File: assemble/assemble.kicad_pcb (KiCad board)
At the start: 2 copper layers, 94 parts, among them J1 Conn_01x04, SW1 SW_Push, SW10 SW_Push, SW11 SW_Push, SW12 SW_Push, SW13 SW_Push, SW14 SW_Push, SW15 SW_Push, SW16 SW_Push, SW17 SW_Push, SW18 SW_Push, SW19 SW_Push, SW2 SW_Push, SW20 SW_Push, SW21 SW_Push, SW22 SW_Push, SW23 SW_Push, SW24 SW_Push, SW25 SW_Push, SW26 SW_Push, SW27 SW_Push, SW28 SW_Push, SW29 SW_Push, SW3 SW_Push, SW30 SW_Push, SW31 SW_Push, SW32 SW_Push, SW33 SW_Push, SW34 SW_Push, SW35 SW_Push, SW36 SW_Push, SW37 SW_Push, SW38 SW_Push, SW39 SW_Push, SW4 SW_Push, SW40 SW_Push, SW41 SW_Push, SW42 SW_Push, SW44 SW_Push, SW45 RotaryEncoder_Switch, SW46 RotaryEncoder_Switch, SW47 SW_SPDT, SW5 SW_Push, SW6 SW_Push, SW7 SW_Push, SW8 SW_Push, SW9 SW_Push

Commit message: feat: re-annotation
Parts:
- moved D1 9.35 mm to (140.9, 58.8), turned to 165 degrees
- moved D5 8.33 mm to (124.9, 52.1), turned to 165 degrees
- moved SW1 8.27 mm to (139.6, 63.8), turned to 165 degrees
- moved SW5 6.84 mm to (123.6, 57.7), turned to 165 degrees
- moved D4 6.68 mm to (136.6, 108.9), turned to 175 degrees
- moved D29 6.58 mm to (233.1, 117.9), turned to -177.5 degrees
- moved SW29 6.50 mm to (232.6, 113.0), turned to 2.5 degrees
- moved SW4 6.50 mm to (137.1, 114.4), turned to 175 degrees
- moved SW13 6.23 mm to (87.2, 49.7), turned to -10 degrees
- moved D2 6.20 mm to (136.3, 74.9), turned to 165 degrees
- moved SW46 6.01 mm to (270.0, 111.0)
- moved D22 6.00 mm to (218.8, 52.5)
- moved D23 6.00 mm to (219.0, 70.0)
- moved D24 6.00 mm to (218.8, 86.5)
- moved D26 6.00 mm to (236.2, 61.2)
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
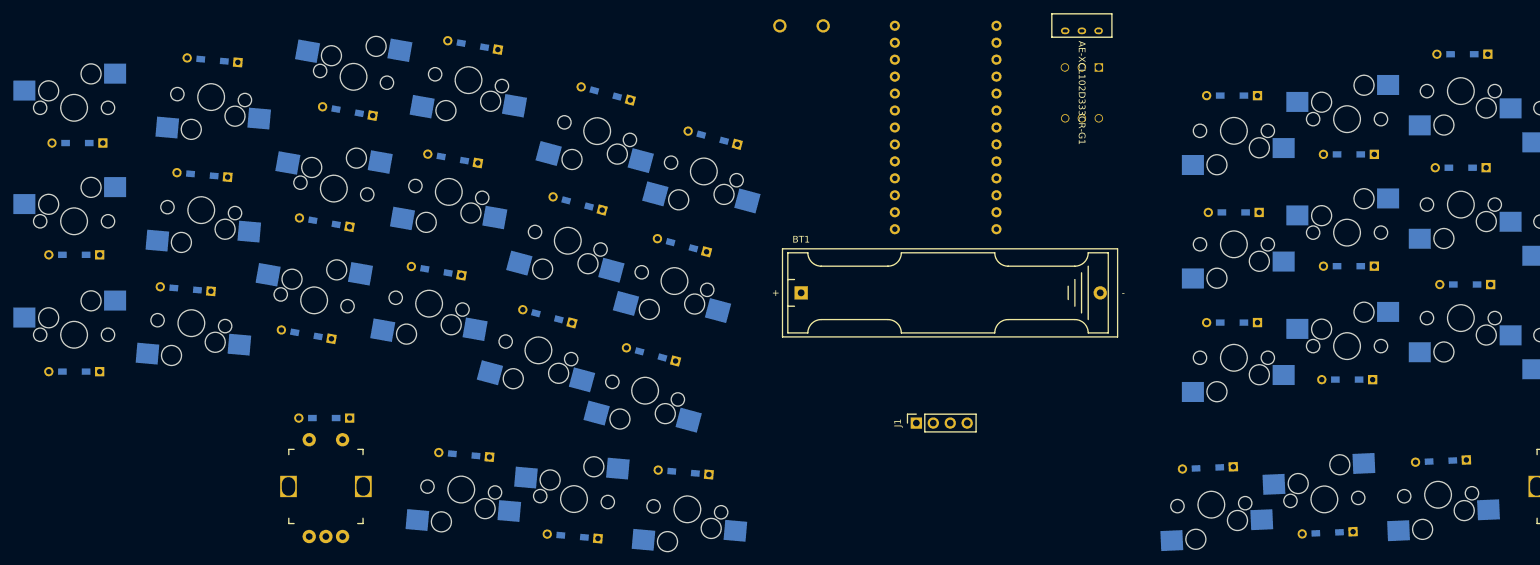
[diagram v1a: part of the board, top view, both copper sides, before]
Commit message: fix: orientations
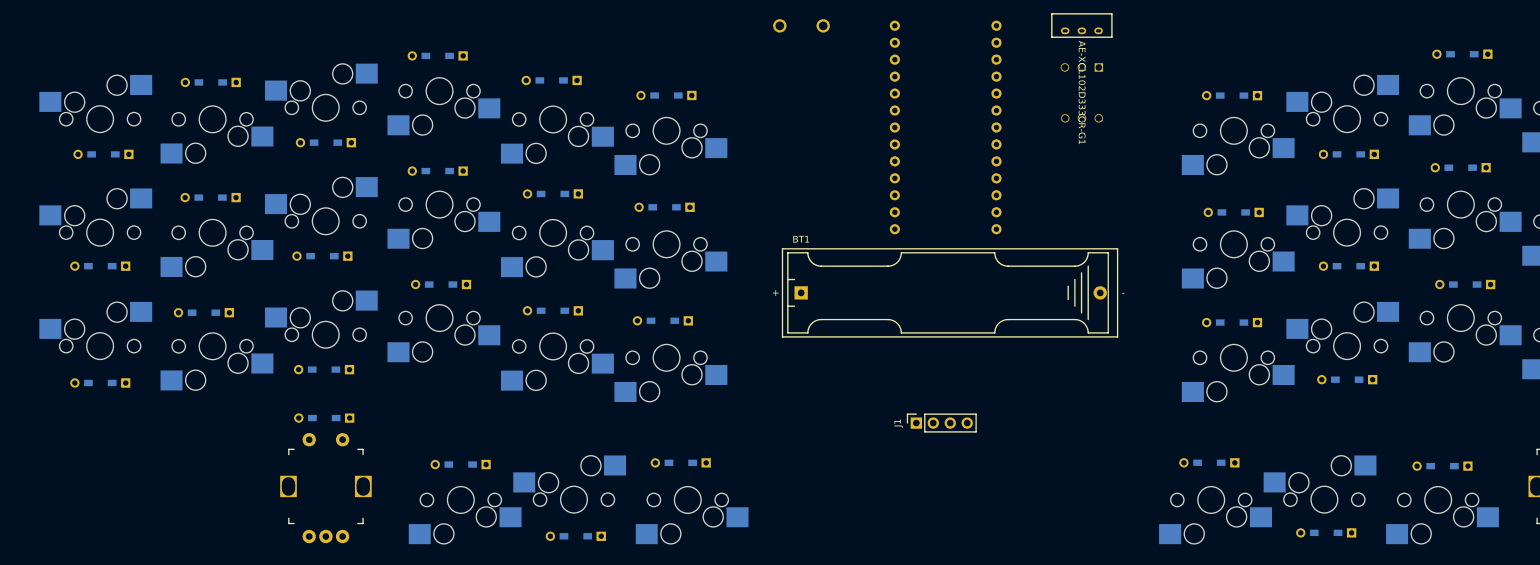
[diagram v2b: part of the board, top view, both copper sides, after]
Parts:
- moved D1 9.39 mm to (134.0, 52.4), turned to 180 degrees
- moved D5 8.34 mm to (116.8, 50.2), turned to 180 degrees
- moved SW1 8.26 mm to (134.0, 57.7), turned to 180 degrees
- moved SW5 6.83 mm to (117.0, 56.0), turned to 180 degrees
- moved D2 6.26 mm to (133.7, 69.2), turned to 180 degrees
- moved SW13 6.23 mm to (83.0, 54.3), turned to 0 degrees
- moved D15 5.90 mm to (82.7, 93.5), turned to 180 degrees
- moved SW3 5.87 mm to (134.0, 91.7), turned to 180 degrees
- moved D13 5.73 mm to (83.0, 59.5), turned to 180 degrees
- moved SW2 5.63 mm to (134.0, 74.7), turned to 180 degrees
- moved D9 5.50 mm to (99.8, 46.5), turned to 180 degrees
- moved SW15 5.44 mm to (83.0, 88.3), turned to 0 degrees
- moved D3 5.35 mm to (133.5, 86.2), turned to 180 degrees
- moved D14 5.08 mm to (82.5, 76.5), turned to 180 degrees
- moved SW14 5.04 mm to (83.0, 71.3), turned to 0 degrees
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
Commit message: feat: add edge cut
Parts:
- moved D25 19.0 mm to (209.1, 125.4), turned to -135 degrees
- moved D4 18.1 mm to (142.8, 124.3), turned to 135 degrees
- moved SW25 16.3 mm to (213.2, 129.1), turned to -135 degrees
- moved SW4 16.1 mm to (139.6, 128.9), turned to 135 degrees
- moved D41 13.4 mm to (307.9, 65.2)
- moved D42 13.3 mm to (307.9, 83.0)
- moved D40 13.2 mm to (308.0, 49.0)
- moved AE-XCL102D333CR-G1 13.2 mm to (193.8, 65.0)
- moved D22 9.44 mm to (211.8, 58.8), turned to -165 degrees
- moved D1 9.36 mm to (141.0, 58.7), turned to 165 degrees
- moved D5 8.35 mm to (125.0, 52.1), turned to 165 degrees
- moved SW22 8.31 mm to (213.4, 63.9), turned to -165 degrees
- moved SW1 8.27 mm to (139.6, 63.8), turned to 165 degrees
- moved SW26 6.85 mm to (229.4, 57.8), turned to 15 degrees
- moved SW5 6.84 mm to (123.6, 57.7), turned to 165 degrees
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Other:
- board outline added: 283.6 x 105.3 mm

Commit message: feat: add switch plate
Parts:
- added R1: R_470k, Resistor_THT:R_Axial_DIN0204_L3.6mm_D1.6mm_P5.08mm_Horizontal, F.Cu at (144.5, 89.0)
- added R2: R_470k, Resistor_THT:R_Axial_DIN0204_L3.6mm_D1.6mm_P5.08mm_Horizontal, F.Cu at (155.5, 89.0)
- added REF**: set_screw_hole, kicad-lib:set_screw_hole, F.Cu at (120.0, 102.2)
- added REF**: set_screw_hole, kicad-lib:set_screw_hole, F.Cu at (12.2, 33.8)
- added REF**: set_screw_hole, kicad-lib:set_screw_hole, F.Cu at (285.0, 34.0)
- added REF**: set_screw_hole, kicad-lib:set_screw_hole, F.Cu at (32.5, 101.8)
- added REF**: set_screw_hole, kicad-lib:set_screw_hole, F.Cu at (185.8, 38.8)
- added REF**: set_screw_hole, kicad-lib:set_screw_hole, F.Cu at (175.0, 102.2)
- added REF**: set_screw_hole, kicad-lib:set_screw_hole, F.Cu at (111.5, 38.8)
- added REF**: set_screw_hole, kicad-lib:set_screw_hole, F.Cu at (264.8, 101.8)
- moved D1 28.6 mm to (112.5, 55.6)
- moved D2 28.6 mm to (107.9, 71.7)
- moved D3 28.6 mm to (103.3, 88.1)
- moved SW1 28.6 mm to (111.2, 60.7)
- moved SW2 28.6 mm to (106.8, 77.1)
- moved SW3 28.6 mm to (102.4, 93.6)
- moved D19 28.5 mm to (17.7, 54.8)
- moved D20 28.5 mm to (17.2, 71.5)
- moved D21 28.5 mm to (17.2, 89.0)
- moved SW19 28.5 mm to (17.2, 49.5)
- moved SW20 28.5 mm to (17.2, 66.5)
- moved SW21 28.5 mm to (17.2, 83.5)
- moved D4 28.4 mm to (114.8, 119.5)
- moved D13 28.4 mm to (58.3, 50.0)
- moved D14 28.4 mm to (54.8, 66.7)
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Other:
- outline, holes or cut-outs redrawn

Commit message: feat: change screw
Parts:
- removed REF** (x8): set_screw_hole, kicad-lib:set_screw_hole
- moved R1 5.56 mm to (139.0, 89.0)
- moved R2 4.69 mm to (150.8, 88.9)

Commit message: feat: wiring
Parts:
- D1, D10, D11, D12, D13, D14, D15, D16, D17, D18, D19, D2, D20, D21, D22, D23, D24, D25, D26, D27, D28, D29, D3, D30, D31, D32, D33, D34, D35, D36, D37, D38, D39, D4, D40, D41, D42, D45, D46, D5, D6, D7, D8, D9: footprint kbd_Parts:Diode_TH_SMD -> kbd_Parts:Diode_SMD
- moved J1 7.95 mm to (151.3, 95.8), turned to -90 degrees
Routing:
- net COL6: track 0.00 -> 510.6 mm, vias 0 -> 11
- net COL4: track 0.00 -> 458.9 mm, vias 0 -> 18
- net COL5: track 0.00 -> 458.8 mm, vias 0 -> 25
- net COL3: track 0.00 -> 422.3 mm, vias 0 -> 23
- net ROW1: track 0.00 -> 421.4 mm, vias 0 -> 32
- net ROW2: track 0.00 -> 380.9 mm, vias 0 -> 24
- net ROW3: track 0.00 -> 364.1 mm, vias 0 -> 19
- net GND: track 0.00 -> 341.9 mm, vias 0 -> 1
- net COL2: track 0.00 -> 333.6 mm, vias 0 -> 22
- net ROW4: track 0.00 -> 329.0 mm, vias 0 -> 17
- net COL1: track 0.00 -> 301.7 mm, vias 0 -> 17
- net RE2A: track 0.00 -> 206.7 mm, vias 0 -> 7
- net RE2B: track 0.00 -> 203.4 mm, vias 0 -> 6
- net RE1A: track 0.00 -> 177.8 mm, vias 0 -> 4
- net RE1B: track 0.00 -> 137.5 mm, vias 0 -> 4
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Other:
- board text added: "ON"
- board text added: "Orbit One v1.0 Designed by derui"

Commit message: fix: screw point
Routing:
- net RE2A: track 206.7 -> 202.8 mm
- net RE2B: track 203.4 -> 202.5 mm
- net GND: track 341.9 -> 341.2 mm

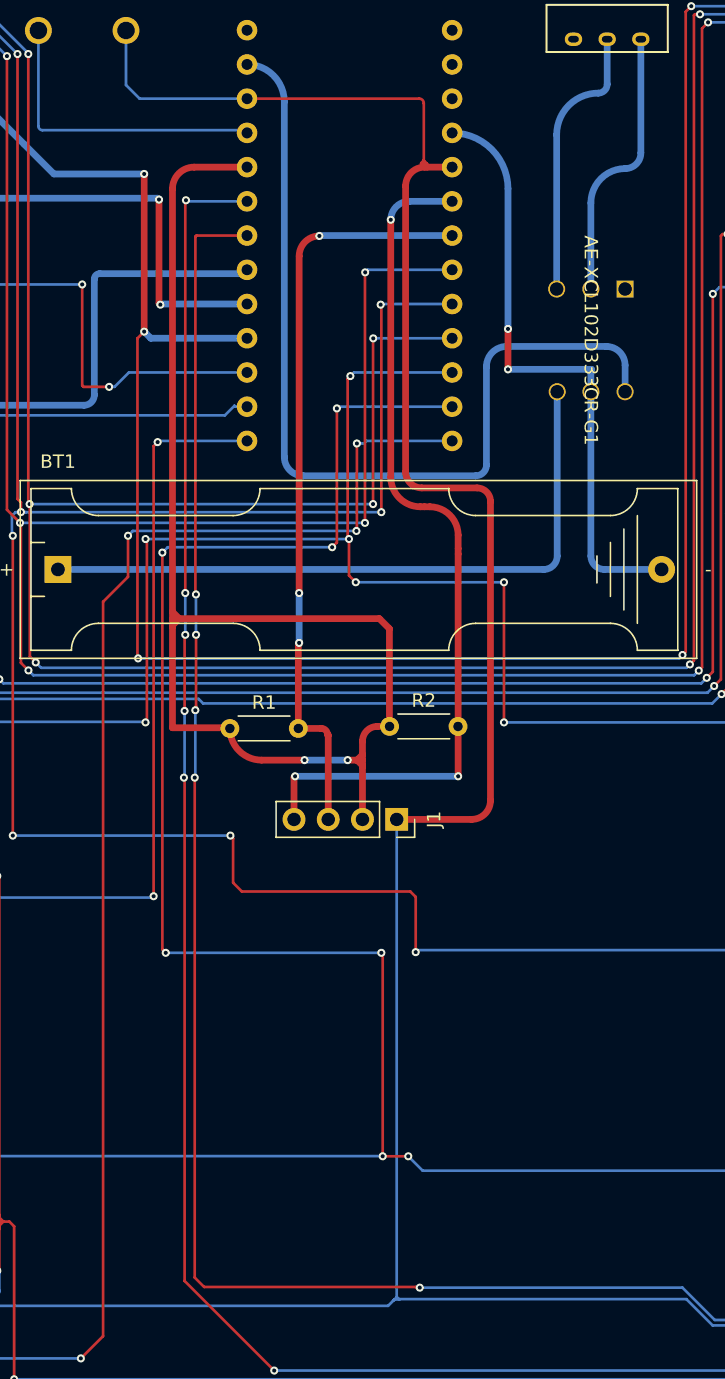
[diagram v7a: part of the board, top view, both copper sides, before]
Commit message: fix: invalid I2C connection
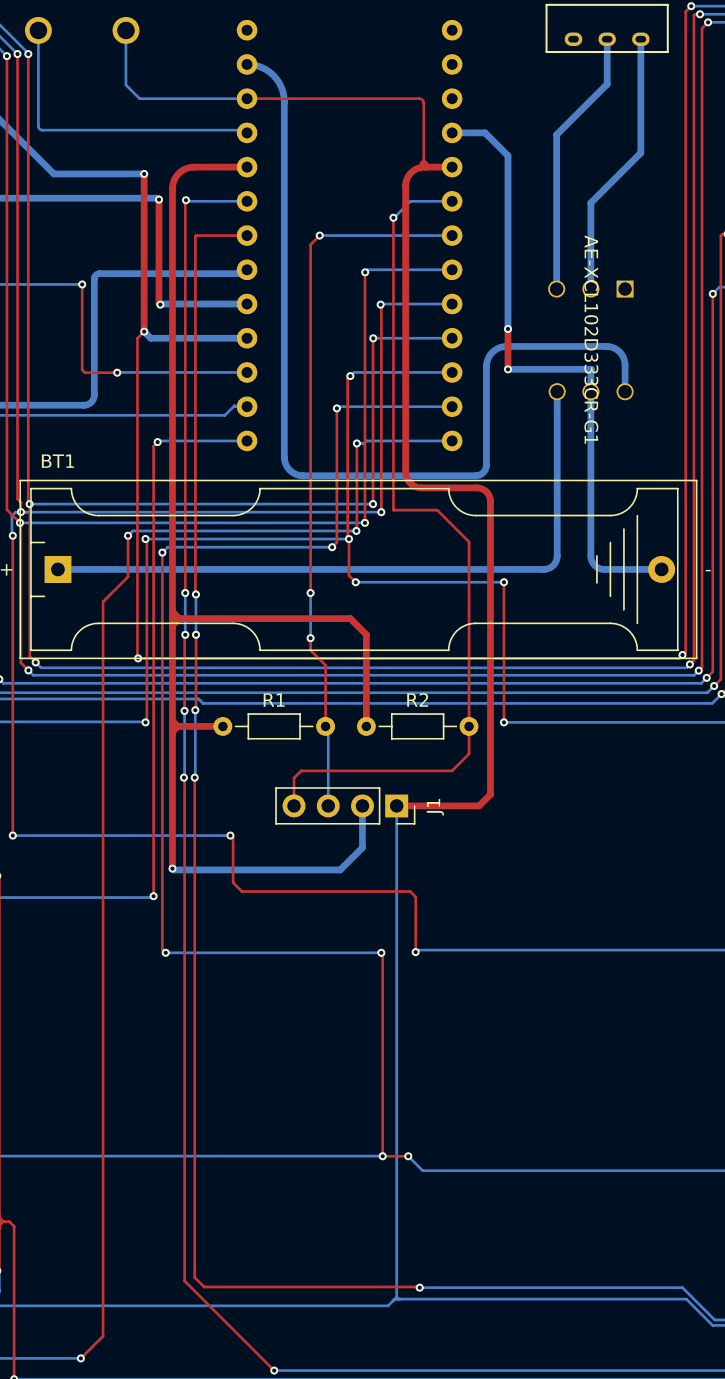
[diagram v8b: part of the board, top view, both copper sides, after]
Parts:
- R1, R2: footprint Resistor_THT:R_Axial_DIN0204_L3.6mm_D1.6mm_P5.08mm_Horizontal -> Resistor_THT:R_Axial_DIN0204_L3.6mm_D1.6mm_P7.62mm_Horizontal
- moved R2 1.72 mm to (149.1, 88.9)
- moved J1 1.00 mm to (151.3, 94.8)
- moved R1 0.54 mm to (138.4, 88.9)
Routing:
- net VCC: track 96.6 -> 103.1 mm, vias 2 -> 1
- net SCL: track 56.0 -> 53.0 mm
- net ROW1: track 421.4 -> 419.8 mm
- net BAT-: track 45.6 -> 46.6 mm
- net SDA: track 64.9 -> 64.7 mm, vias 3 -> 1
